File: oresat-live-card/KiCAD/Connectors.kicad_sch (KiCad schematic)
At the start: 32 parts, among them J1 ORESAT-DEBUG-CONNECTOR-CARD, J4 TFM-120-01-L-D-RA, J6 J-MOLEX-SMPM-73300-003X, J8 J-MOLEX-SMPM-73300-003X

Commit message: added RF scwitches
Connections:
- net TURNSTILE_ANTENNA: now reaches J8.SIG
- net TX_OUT renamed HELIX_ANTENNA
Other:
- moved on the sheet: J8
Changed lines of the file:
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@@
 	(text "OreSat Power Domain signals\n(See power sheet)"
 		(exclude_from_sim no)
-		(at 177.8 109.22 0)
+		(at 175.26 110.49 0)
 		(effects
 			(font
@@
 	)
 	(junction
-		(at 138.43 106.68)
+		(at 138.43 107.95)
 		(diameter 0)
 		(color 0 0 0 0)
@@
 	(wire
 		(pts
-			(xy 323.85 193.04) (xy 323.85 196.85)
+			(xy 307.34 191.77) (xy 307.34 195.58)
 		)
 		(stroke
@@
 	(wire
 		(pts
-			(xy 138.43 109.22) (xy 138.43 106.68)
+			(xy 138.43 109.22) (xy 138.43 107.95)
 		)
 		(stroke
@@
 	(wire
 		(pts
-			(xy 154.94 109.22) (xy 144.78 109.22)
-		)
-		(stroke
-			(width 0)
-			(type default)
-		)
-	)
-	(wire
-		(pts
 			(xy 138.43 144.78) (xy 138.43 147.32)
 		)
@@
 	(wire
 		(pts
-			(xy 144.78 111.76) (xy 138.43 111.76)
+			(xy 138.43 111.76) (xy 154.94 111.76)
 		)
 		(stroke
@@
 	(polyline
 		(pts
-			(xy 170.18 101.6) (xy 172.72 101.6)
+			(xy 170.18 102.87) (xy 172.72 102.87)
 		)
 		(stroke
@@
 	(polyline
 		(pts
-			(xy 172.72 111.76) (xy 170.18 111.76)
+			(xy 172.72 113.03) (xy 170.18 113.03)
 		)
 		(stroke
@@
 	(wire
 		(pts
+			(xy 297.18 186.69) (xy 302.26 186.69)
+		)
+		(stroke
+			(width 0)
+			(type default)
+		)
+	)
+	(wire
+		(pts
 			(xy 132.08 129.54) (xy 144.78 129.54)
 		)
@@
 	(wire
 		(pts
-			(xy 154.94 106.68) (xy 138.43 106.68)
+			(xy 154.94 107.95) (xy 138.43 107.95)
 		)
 		(stroke
@@
 	(wire
 		(pts
-			(xy 144.78 109.22) (xy 144.78 111.76)
-		)
-		(stroke
-			(width 0)
-			(type default)
-		)
-	)
-	(wire
-		(pts
 			(xy 132.08 157.48) (xy 138.43 157.48)
 		)
@@
 	(wire
 		(pts
+			(xy 138.43 107.95) (xy 138.43 106.68)
+		)
+		(stroke
+			(width 0)
+			(type default)
+		)
+	)
+	(wire
+		(pts
 			(xy 276.86 142.24) (xy 287.02 142.24)
 		)
@@
 	(polyline
 		(pts
-			(xy 172.72 101.6) (xy 172.72 111.76)
+			(xy 172.72 102.87) (xy 172.72 113.03)
 		)
 		(stroke
@@
 	(global_label "OPD_PWR"
 		(shape input)
-		(at 154.94 109.22 0)
+		(at 154.94 111.76 0)
 		(fields_autoplaced yes)
 		(effects
@@
 		)
 		(property "Intersheetrefs" "${INTERSHEET_REFS}"
-			(at 166.1826 109.1406 0)
+			(at 166.1826 111.6806 0)
 			(effects
 				(font
@@
 	(global_label "OPD_SCL"
 		(shape input)
-		(at 154.94 106.68 0)
+		(at 154.94 107.95 0)
 		(fields_autoplaced yes)
 		(effects
@@
 		)
 		(property "Intersheetrefs" "${INTERSHEET_REFS}"
-			(at 165.6988 106.6006 0)
+			(at 165.6988 107.8706 0)
 			(effects
 				(font
@@
 		)
 	)
+	(global_label "TURNSTILE_ANTENNA"
+		(shape input)
+		(at 297.18 186.69 180)
+		(fields_autoplaced yes)
+		(effects
+			(font
+				(size 1.27 1.27)
+			)
+			(justify right)
+		)
+		(property "Intersheetrefs" "${INTERSHEET_REFS}"
+			(at 275.0843 186.69 0)
+			(effects
+				(font
+					(size 1.27 1.27)
+				)
+				(justify right)
+			)
+		)
+	)
 	(global_label "Spare2"
 		(shape input)
@@
 		)
 	)
-	(global_label "TX_OUT"
+	(global_label "HELIX_ANTENNA"
 		(shape input)
 		(at 297.18 165.1 180)
@@
 		(effects
 			(font
-				(size 0.889 0.889)
+				(size 1.27 1.27)
 			)
 			(justify right)
 		)
 		(property "Intersheetrefs" "${INTERSHEET_REFS}"
-			(at 290.7496 165.0445 0)
+			(at 284.8884 165.1 0)
 			(effects
 				(font
@@
 	(symbol
 		(lib_id "oresat-connectors:J-MOLEX-SMPM-73300-002X")
-		(at 323.85 187.96 0)
+		(at 307.34 186.69 0)
 		(mirror y)
 		(unit 1)
@@
 		(dnp no)
 		(property "Reference" "J8"
-			(at 318.77 191.77 0)
+			(at 302.26 190.5 0)
 			(effects
 				(font
@@
 		)
 		(property "Value" "J-MOLEX-SMPM-73300-003X"
-			(at 318.77 194.31 0)
+			(at 302.26 193.04 0)
 			(effects
 				(font
@@
 		)
 		(property "Footprint" "oresat-connectors:J-MOLEX-SMPM-073300-002X"
-			(at 323.85 181.61 0)
+			(at 307.34 180.34 0)
 			(effects
 				(font
@@
 		)
 		(property "Datasheet" "https://tools.molex.com/pdm_docs/sd/733000020_sd.pdf"
-			(at 323.85 179.07 0)
+			(at 307.34 177.8 0)
 			(effects
 				(font
@@
 		)
 		(property "Description" "CONN SMPM PLUG STR EDGEMNT"
-			(at 323.85 181.61 0)
+			(at 307.34 180.34 0)
 			(effects
 				(font
@@
 		)
 		(property "MPN" "0733000020"
-			(at 323.85 180.34 0)
+			(at 307.34 179.07 0)
 			(effects
 				(font
@@
 		)
 		(property "Distributor" "DigiKey"
-			(at 323.85 179.07 0)
+			(at 307.34 177.8 0)
 			(effects
 				(font
@@
 	(symbol
 		(lib_id "power:GND")
-		(at 323.85 196.85 0)
+		(at 307.34 195.58 0)
 		(unit 1)
 		(exclude_from_sim no)
@@
 		(fields_autoplaced yes)
 		(property "Reference" "#PWR05"
-			(at 323.85 203.2 0)
+			(at 307.34 201.93 0)
 			(effects
 				(font
@@
 		)
 		(property "Value" "GND"
-			(at 323.85 201.93 0)
+			(at 307.34 200.66 0)
 			(effects
 				(font
@@
 		)
 		(property "Footprint" ""
-			(at 323.85 196.85 0)
+			(at 307.34 195.58 0)
 			(effects
 				(font
@@
 		)
 		(property "Datasheet" ""
-			(at 323.85 196.85 0)
+			(at 307.34 195.58 0)
 			(effects
 				(font
@@
 		)
 		(property "Description" "Power symbol creates a global label with name \"GND\" , ground"
-			(at 323.85 196.85 0)
+			(at 307.34 195.58 0)
 			(effects
 				(font

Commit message: implemented notes from Oliver. Added notes for self to fix later
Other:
- note added: "WHY IS THIS TEXT SMALLER?"
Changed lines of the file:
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@@
 	(title_block
 		(title "Oresat DxWifi Card")
-		(date "2025-04-25")
+		(date "2025-05-28")
 		(rev "2")
 	)
@@
 		)
 	)
+	(text "WHY IS THIS TEXT SMALLER?\n"
+		(exclude_from_sim no)
+		(at 272.542 162.56 0)
+		(effects
+			(font
+				(size 1.27 1.27)
+			)
+		)
+	)
 	(junction
 		(at 138.43 107.95)
@@
 	(wire
 		(pts
-			(xy 302.26 165.1) (xy 297.18 165.1)
-		)
-		(stroke
-			(width 0)
-			(type default)
-		)
-	)
-	(wire
-		(pts
 			(xy 138.43 165.1) (xy 138.43 162.56)
 		)
@@
 	(wire
 		(pts
+			(xy 297.18 165.1) (xy 302.26 165.1)
+		)
+		(stroke
+			(width 0)
+			(type default)
+		)
+	)
+	(wire
+		(pts
 			(xy 138.43 139.7) (xy 138.43 137.16)
 		)
@@
 		)
 		(property "Intersheetrefs" "${INTERSHEET_REFS}"
-			(at 284.8884 165.1 0)
-			(effects
-				(font
+			(at 279.62 165.1 0)
+			(effects
+				(font

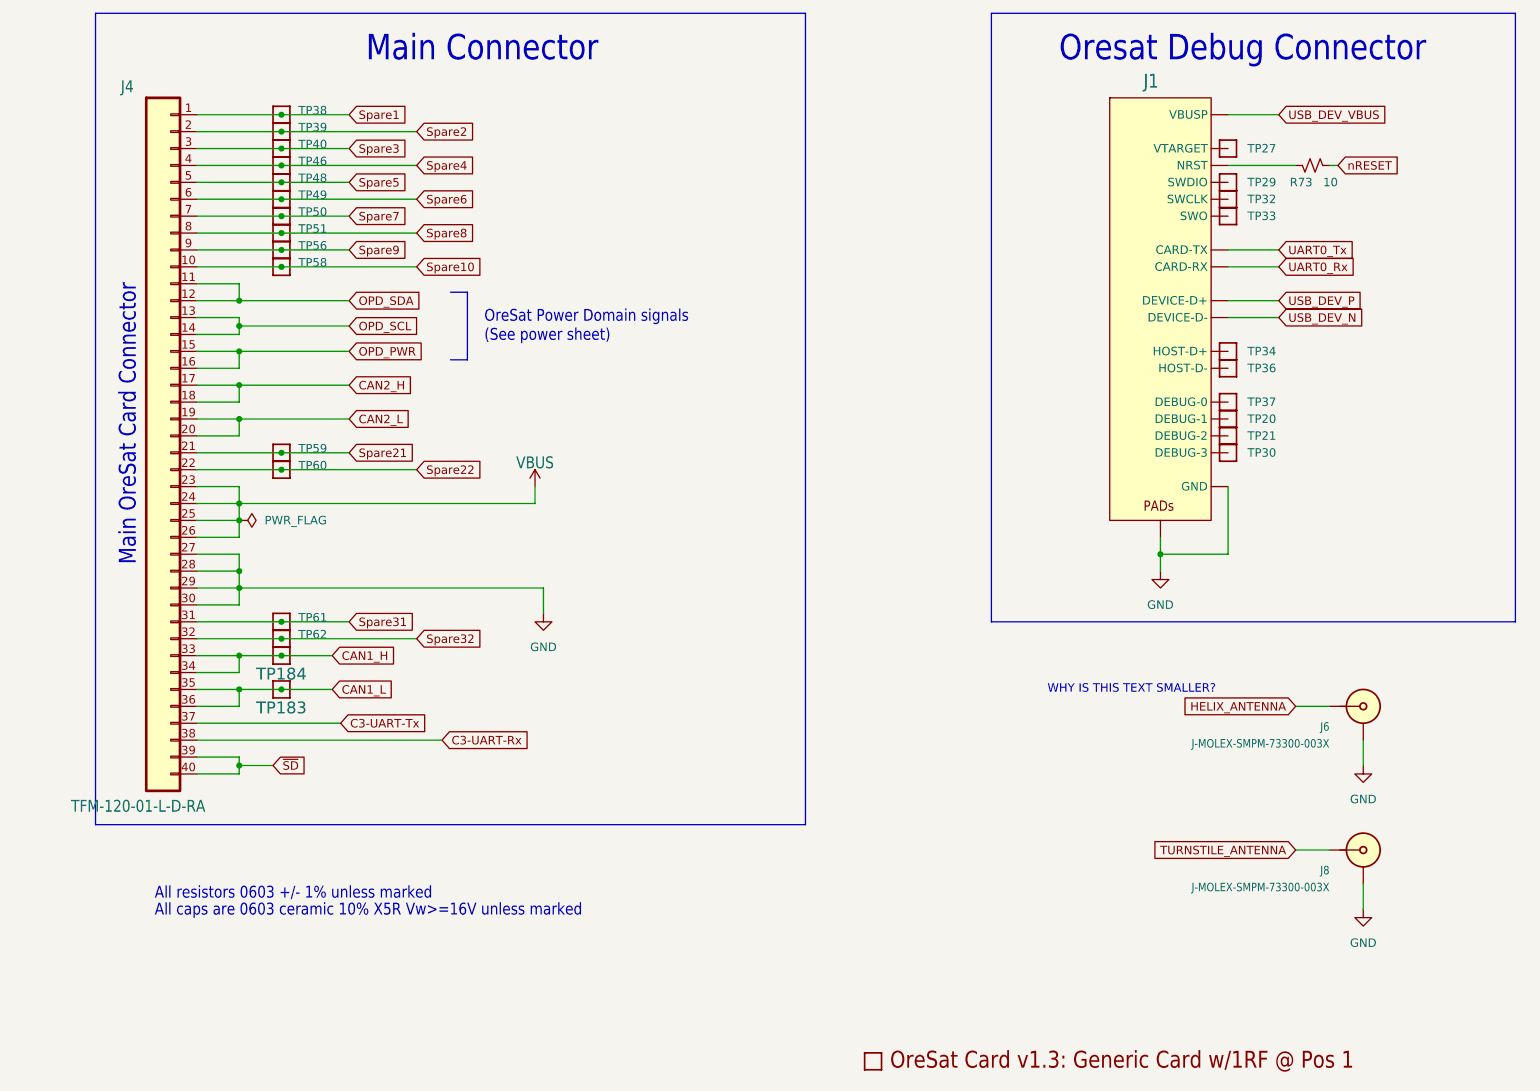
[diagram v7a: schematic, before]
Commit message: Fixed up schematic as best as possible. There were a lot of issues with local paths being referenced, and EAGLE import libraries. Fixed all of those, as well as fixed some oresat-kicad IC symbols (bad direction pins) and I think we're now OK. Also updated card outline for two RF (LEFT) connectors.  Still missing two packages, but we'll deal with that later.
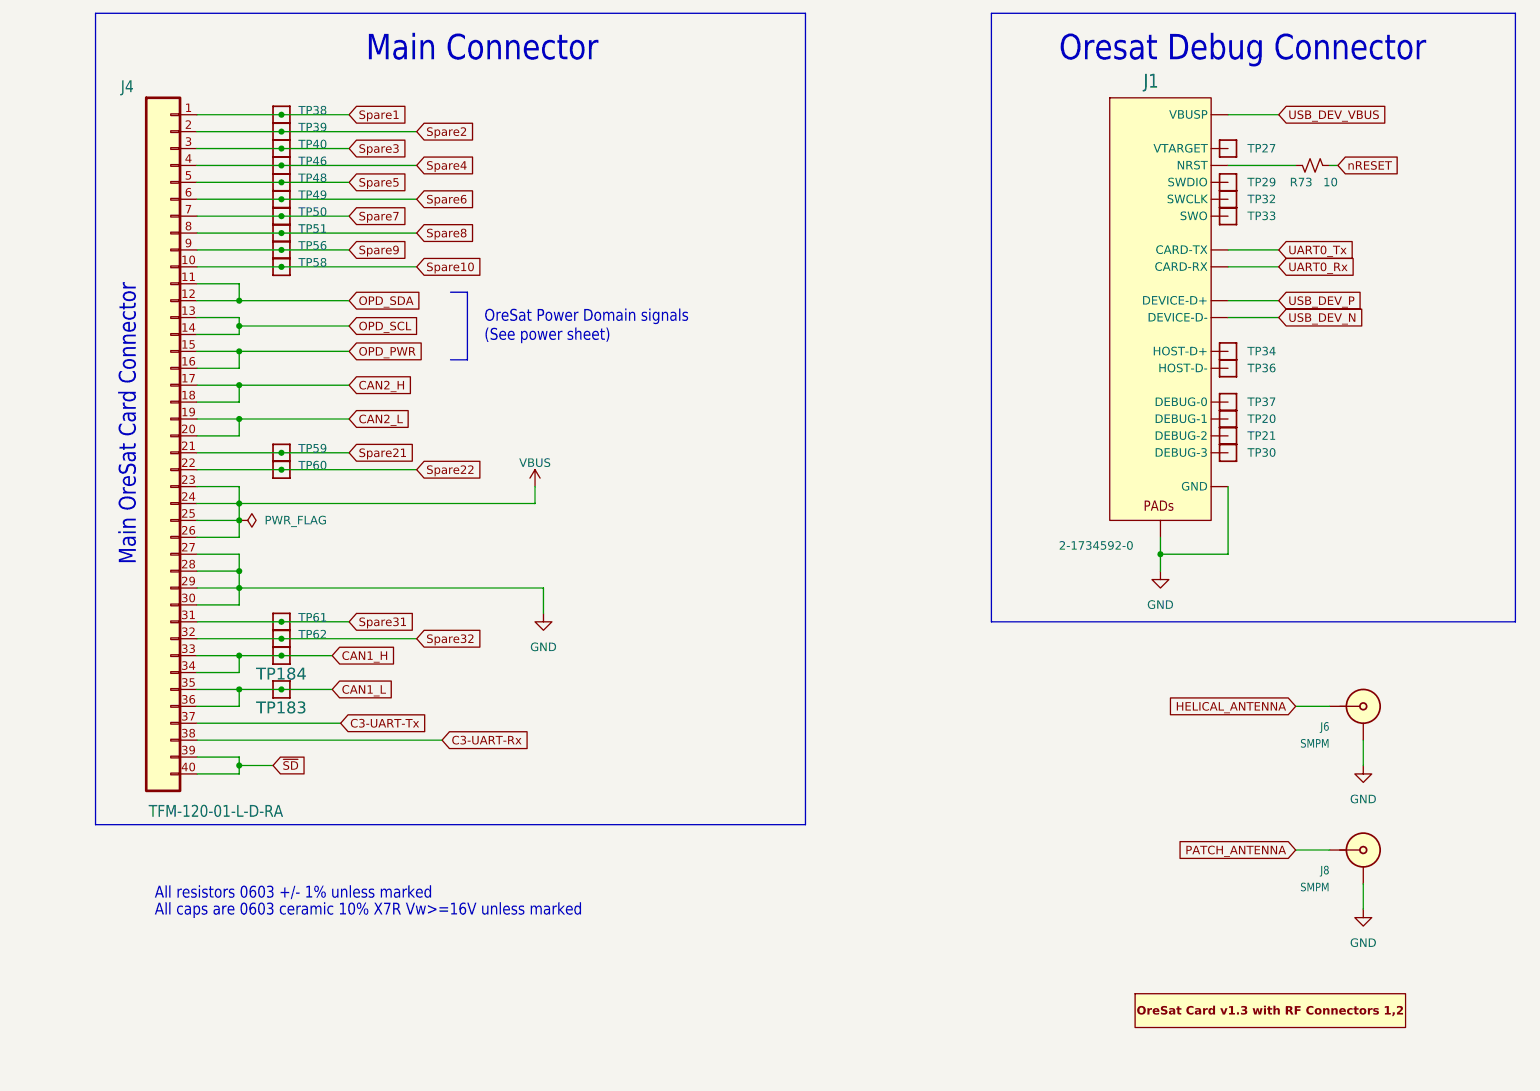
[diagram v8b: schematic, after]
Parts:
- J1: value ORESAT-DEBUG-CONNECTOR-CARD -> ORESAT-DEBUG-CONNECTOR; DPN (none) -> A100287CT-ND; MFR (none) -> TE Connectivity AMP Connectors
- J4: DPN (none) -> SAM10145-ND; MFR (none) -> Samtec Inc.
- J6, J8: value J-MOLEX-SMPM-73300-003X -> SMPM; DPN (none) -> WM10772-ND; MFR (none) -> MOLEX
- PCB1: footprint oresat-live-card:ORESAT-CARD-V1.3-GENERIC-1RF-POS1 -> oresat-pcbs:ORESAT-CARD-V1.3-2RF-LEFT; symbol oresat-live-card-eagle-import:ORESAT-CARD-V1.3-GENERIC-1RF-POS1 -> oresat-pcbs:ORESAT-CARD-V1.3-2RF-LEFT
- R73: DPN (none) -> P10.0HCT-ND; Distributor (none) -> DigiKey; MFR (none) -> Panasonic; MPN (none) -> ERJ-3EKF10R0V
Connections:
- net HELIX_ANTENNA renamed HELICAL_ANTENNA
- net TURNSTILE_ANTENNA renamed PATCH_ANTENNA
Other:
- note added: "All caps are 0603 ceramic 10% X7R Vw>=16V unless marked"
- note removed: "All caps are 0603 ceramic 10% X5R Vw>=16V unless marked"
- note removed: "WHY IS THIS TEXT SMALLER?"
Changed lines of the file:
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@@
 		)
 	)
-	(text "All caps are 0603 ceramic 10% X5R Vw>=16V unless marked"
+	(text "All caps are 0603 ceramic 10% X7R Vw>=16V unless marked"
 		(exclude_from_sim no)
 		(at 125.73 196.85 0)
@@
 		)
 	)
-	(text "WHY IS THIS TEXT SMALLER?\n"
-		(exclude_from_sim no)
-		(at 272.542 162.56 0)
-		(effects
-			(font
-				(size 1.27 1.27)
-			)
-		)
-	)
 	(junction
 		(at 138.43 107.95)
@@
 		)
 	)
-	(global_label "TURNSTILE_ANTENNA"
+	(global_label "PATCH_ANTENNA"
 		(shape input)
 		(at 297.18 186.69 180)
@@
 		)
 		(property "Intersheetrefs" "${INTERSHEET_REFS}"
-			(at 275.0843 186.69 0)
+			(at 279.0152 186.69 0)
 			(effects
 				(font
@@
 		)
 	)
-	(global_label "HELIX_ANTENNA"
+	(global_label "HELICAL_ANTENNA"
 		(shape input)
 		(at 297.18 165.1 180)
@@
 		)
 		(property "Intersheetrefs" "${INTERSHEET_REFS}"
-			(at 279.62 165.1 0)
+			(at 277.4428 165.1 0)
 			(effects
 				(font
-					(size 0.889 0.889)
+					(size 1.27 1.27)
 				)
 				(justify right)
@@
 	)
 	(symbol
-		(lib_id "oresat-live-card-eagle-import:ORESAT-CARD-V1.3-GENERIC-1RF-POS1")
-		(at 233.68 218.44 0)
+		(lib_id "oresat-pcbs:ORESAT-CARD-V1.3-2RF-LEFT")
+		(at 293.37 210.82 0)
 		(unit 1)
 		(exclude_from_sim no)
@@
 		(dnp no)
 		(property "Reference" "PCB1"
-			(at 233.68 218.44 0)
+			(at 293.37 210.82 0)
 			(effects
 				(font
@@
 		)
 		(property "Value" "ORESAT-CARD-V1.3-GENERIC-1RF-POS1"
-			(at 233.68 218.44 0)
+			(at 293.37 210.82 0)
 			(effects
 				(font
@@
 			)
 		)
-		(property "Footprint" "oresat-live-card:ORESAT-CARD-V1.3-GENERIC-1RF-POS1"
-			(at 233.68 218.44 0)
+		(property "Footprint" "oresat-pcbs:ORESAT-CARD-V1.3-2RF-LEFT"
+			(at 293.37 199.39 0)
 			(effects
 				(font
@@
 		)
 		(property "Datasheet" ""
-			(at 233.68 218.44 0)
+			(at 293.37 210.82 0)
 			(effects
 				(font
@@
 		)
 		(property "Description" ""
-			(at 233.68 218.44 0)
+			(at 293.37 210.82 0)
 			(effects
 				(font
@@
 			)
 		)
-		(property "Description" ""
+		(property "Description" "RES SMD 10 OHM 1% 1/10W 0603"
 			(at 299.72 83.82 0)
 			(effects
@@
 			)
 		)
+		(property "DPN" "P10.0HCT-ND "
+			(at 299.72 83.82 90)
+			(effects
+				(font
+					(size 1.27 1.27)
+				)
+				(hide yes)
+			)
+		)
+		(property "Distributor" "DigiKey"
+			(at 299.72 83.82 90)
+			(effects
+				(font
+					(size 1.27 1.27)
+				)
+				(hide yes)
+			)
+		)
+		(property "MFR" "Panasonic "
+			(at 299.72 83.82 90)
+			(effects
+				(font
+					(size 1.27 1.27)
+				)
+				(hide yes)
+			)
+		)
+		(property "MPN" "ERJ-3EKF10R0V "
+			(at 299.72 83.82 90)
+			(effects
+				(font
+					(size 1.27 1.27)
+				)
+				(hide yes)
+			)
+		)
 		(pin "1"
 		)
@@
 		)
 		(property "Value" "TFM-120-01-L-D-RA"
-			(at 133.35 179.07 0)
+			(at 145.034 179.832 0)
 			(effects
 				(font
@@
 			)
 		)
+		(property "DPN" "SAM10145-ND "
+			(at 127 124.46 0)
+			(effects
+				(font
+					(size 1.27 1.27)
+				)
+				(hide yes)
+			)
+		)
+		(property "MFR" "Samtec Inc. "
+			(at 127 124.46 0)
+			(effects
+				(font
+					(size 1.27 1.27)
+				)
+				(hide yes)
+			)
+		)
 		(pin "1"
 		)
@@
 		(dnp no)
 		(fields_autoplaced yes)
-		(property "Reference" "#PWR03"
+		(property "Reference" "#PWR3"
 			(at 276.86 151.13 0)
 			(effects
@@
 			(project "oresat-live-card"
 				(path "/748bdd2d-da0a-4240-ba60-0bf881d2ec56/1bdb8d5b-8060-49dd-b753-8985e7684076"
-					(reference "#PWR03")
+					(reference "#PWR3")
 					(unit 1)
 				)
@@
 	)
 	(symbol
-		(lib_id "oresat-power:VBUS")
+		(lib_id "power:VBUS")
 		(at 182.88 132.08 0)
 		(unit 1)
@@
 		(on_board yes)
 		(dnp no)
-		(property "Reference" "#VBUS0101"
-			(at 182.88 132.08 0)
+		(property "Reference" "#PWR101"
+			(at 182.88 135.89 0)
 			(effects
 				(font
@@
 		)
 		(property "Value" "VBUS"
-			(at 182.88 129.54 0)
+			(at 182.88 128.524 0)
 			(effects
 				(font
-					(size 1.778 1.5113)
+					(size 1.27 1.27)
 				)
-				(justify bottom)
 			)
 		)
@@
 			)
 		)
-		(property "Description" ""
+		(property "Description" "Power symbol creates a global label with name \"VBUS\""
 			(at 182.88 132.08 0)
 			(effects
@@
 			(project "oresat-live-card"
 				(path "/748bdd2d-da0a-4240-ba60-0bf881d2ec56/1bdb8d5b-8060-49dd-b753-8985e7684076"
-					(reference "#VBUS0101")
+					(reference "#PWR101")
 					(unit 1)
 				)
@@
 			)
 		)
-		(property "Value" "ORESAT-DEBUG-CONNECTOR-CARD"
+		(property "Value" "ORESAT-DEBUG-CONNECTOR"
 			(at 276.86 104.14 0)
 			(effects
@@
 		)
 		(property "MPN" "2-1734592-0"
+			(at 267.208 140.97 0)
+			(effects
+				(font
+					(size 1.27 1.27)
+				)
+			)
+		)
+		(property "Distributor" "DigiKey"
 			(at 276.86 104.14 0)
 			(effects
@@
 			)
 		)
-		(property "Distributor" "DigiKey"
+		(property "DPN" "A100287CT-ND "
+			(at 276.86 104.14 0)
+			(effects
+				(font
+					(size 1.27 1.27)
+				)
+				(hide yes)
+			)
+		)
+		(property "MFR" "TE Connectivity AMP Connectors "
 			(at 276.86 104.14 0)
 			(effects
@@
 			)
 		)
-		(property "Value" "J-MOLEX-SMPM-73300-003X"
+		(property "Value" "SMPM"
 			(at 302.26 193.04 0)
 			(effects
@@
 			)
 		)
-		(property "Description" "CONN SMPM PLUG STR EDGEMNT"
+		(property "Description" "CONN SMPM PLUG STR 50OHM EDGEMNT"
 			(at 307.34 180.34 0)
 			(effects
@@
 			)
 		)
+		(property "DPN" "WM10772-ND "
+			(at 307.34 186.69 0)
+			(effects
+				(font
+					(size 1.27 1.27)
+				)
+				(hide yes)
+			)
+		)
+		(property "MFR" "MOLEX"
+			(at 307.34 186.69 0)
+			(effects
+				(font
+					(size 1.27 1.27)
+				)
+				(hide yes)
+			)
+		)
 		(pin "SIG"
 		)
@@
 		(dnp no)
 		(fields_autoplaced yes)
-		(property "Reference" "#PWR02"
+		(property "Reference" "#PWR2"
 			(at 184.15 157.48 0)
 			(effects
@@
 			(project "oresat-live-card"
 				(path "/748bdd2d-da0a-4240-ba60-0bf881d2ec56/1bdb8d5b-8060-49dd-b753-8985e7684076"
-					(reference "#PWR02")
+					(reference "#PWR2")
 					(unit 1)
 				)
@@
 		(dnp no)
 		(fields_autoplaced yes)
-		(property "Reference" "#PWR04"
+		(property "Reference" "#PWR4"
 			(at 307.34 180.34 0)
 			(effects
@@
 			(project "oresat-live-card"
 				(path "/748bdd2d-da0a-4240-ba60-0bf881d2ec56/1bdb8d5b-8060-49dd-b753-8985e7684076"
-					(reference "#PWR04")
+					(reference "#PWR4")
 					(unit 1)
 				)
@@
 			)
 		)
-		(property "Value" "J-MOLEX-SMPM-73300-003X"
+		(property "Value" "SMPM"
 			(at 302.26 171.45 0)
 			(effects
@@
 			)
 		)
-		(property "Description" "CONN SMPM PLUG STR EDGEMNT"
+		(property "Description" "CONN SMPM PLUG STR 50OHM EDGEMNT"
 			(at 307.34 158.75 0)
 			(effects
@@
 			)
 		)
+		(property "DPN" "WM10772-ND "
+			(at 307.34 165.1 0)
+			(effects
+				(font
+					(size 1.27 1.27)
+				)
+				(hide yes)
+			)
+		)
+		(property "MFR" "MOLEX"
+			(at 307.34 165.1 0)
+			(effects
+				(font
+					(size 1.27 1.27)
+				)
+				(hide yes)
+			)
+		)
 		(pin "SIG"
 		)
@@
 		(dnp no)
 		(fields_autoplaced yes)
-		(property "Reference" "#PWR05"
+		(property "Reference" "#PWR5"
 			(at 307.34 201.93 0)
 			(effects
@@
 			(project "oresat-live-card"
 				(path "/748bdd2d-da0a-4240-ba60-0bf881d2ec56/1bdb8d5b-8060-49dd-b753-8985e7684076"
-					(reference "#PWR05")
+					(reference "#PWR5")
 					(unit 1)
 				)
